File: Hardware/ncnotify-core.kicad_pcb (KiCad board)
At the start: 4 copper layers, 62.5 x 32.5 mm, 48 parts, among them J1 5-1634503-1, J2 67996-412HLF, J3 USB4110-GF-A, J4 Conn_ARM_JTAG_SWD_10, Q1 NX3008NBKS, SW1 SW_Push, SW2 SW_Push, U1 STM32L422CBT6, U2 TLV71333PDBV, X1 SMTU1632-LF, Y1 Q13FC1350000400

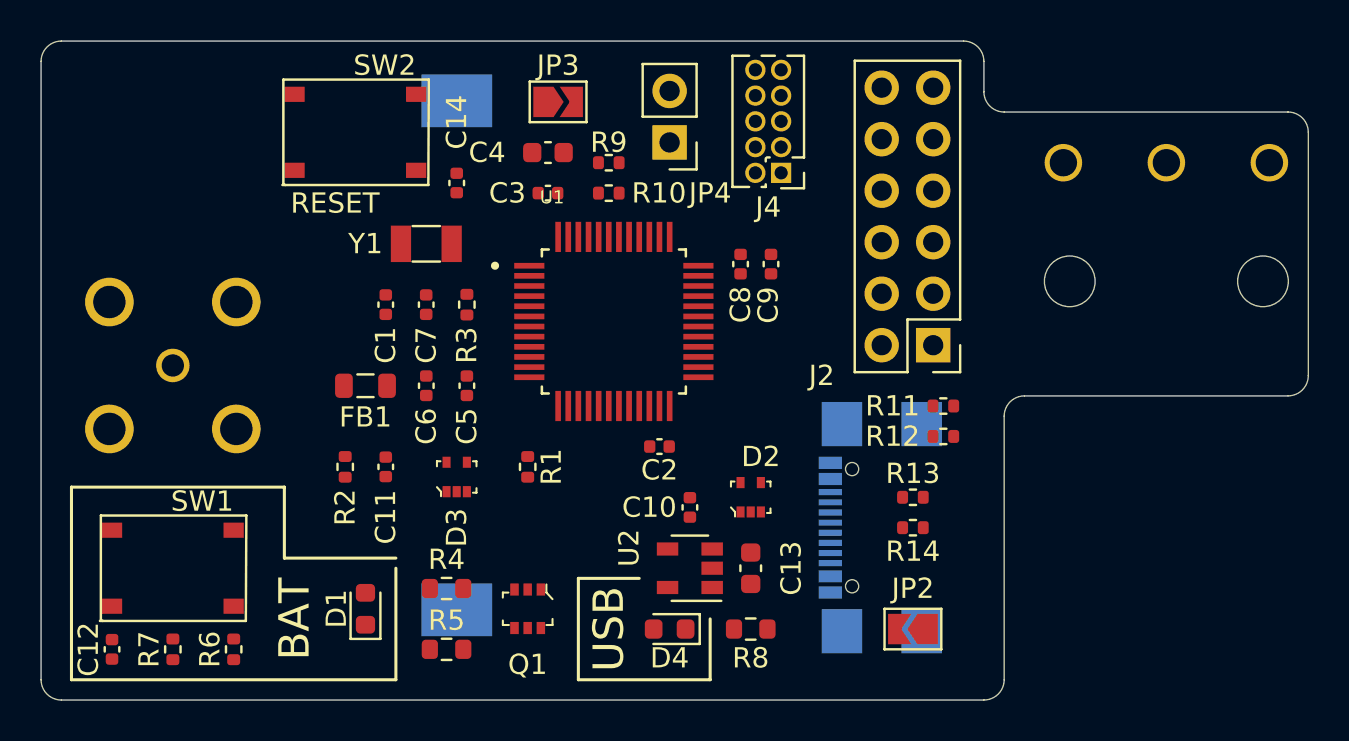
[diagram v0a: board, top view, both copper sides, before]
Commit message: Remove switches and expansion header
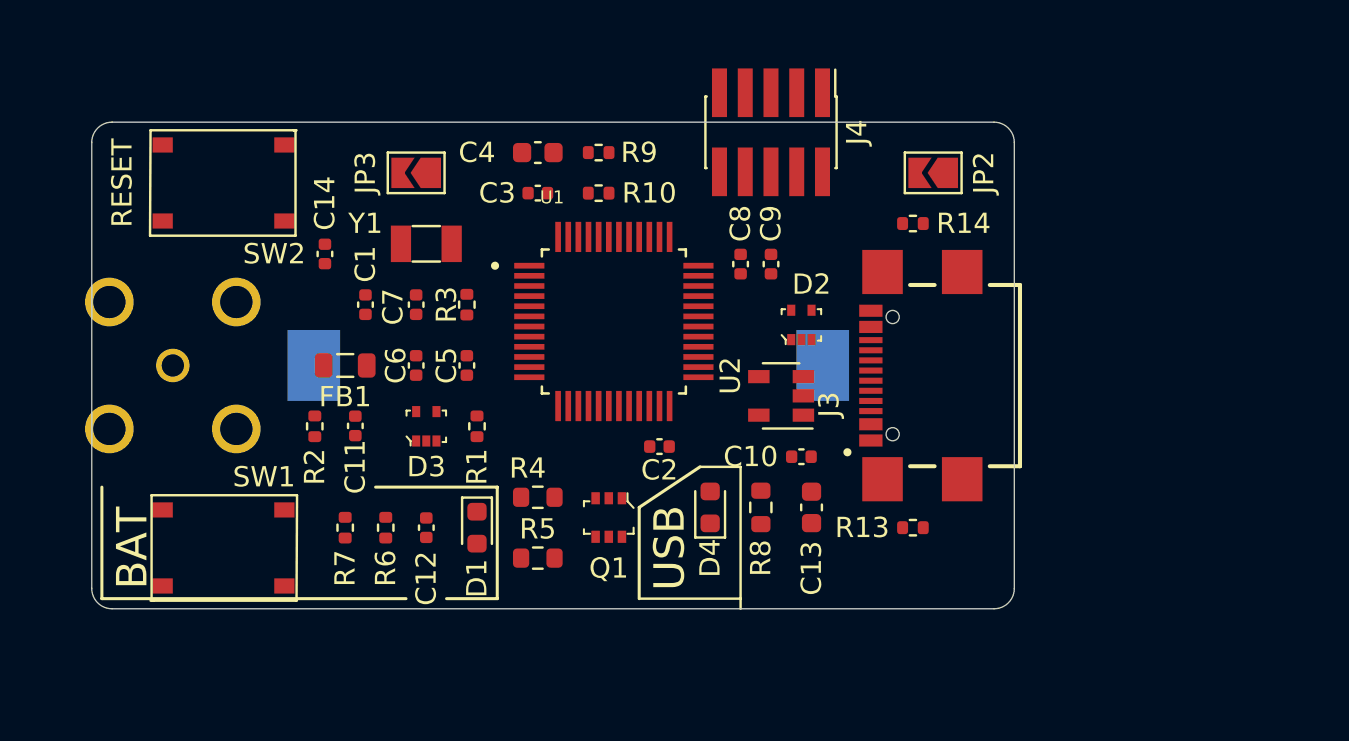
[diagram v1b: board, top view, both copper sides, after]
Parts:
- removed J2: 67996-412HLF, Connector_PinHeader_2.54mm:PinHeader_2x06_P2.54mm_Vertical
- removed JP4: Jumper_2_Open, Connector_PinHeader_2.54mm:PinHeader_1x02_P2.54mm_Vertical
- removed R11, R12: 5k1, Resistor_SMD:R_0402_1005Metric
- removed S1: ZMSL03130T10LLC, ncnotify-core:ZMSL03130T10LLC
- J3: moved to F.Cu
- J4: footprint Connector_PinHeader_1.27mm:PinHeader_2x05_P1.27mm_Vertical -> Connector_PinHeader_1.27mm:PinHeader_2x05_P1.27mm_Vertical_SMD
- moved JP2 22.5 mm to (249.0, -47.5)
- moved C12 16.6 mm to (224.0, -30.0), turned to 270 degrees
- moved R14 15.0 mm to (248.0, -45.0), turned to 0 degrees
- moved R7 10.4 mm to (220.0, -30.0), turned to 270 degrees
- moved U2 9.62 mm to (241.5, -36.5)
- moved R6 9.60 mm to (222.0, -30.0), turned to 270 degrees
- moved D2 8.86 mm to (242.5, -40.0)
- moved JP3 7.83 mm to (223.5, -47.5), turned to 180 degrees
- moved J3 7.76 mm to (247.0, -37.5), turned to 90 degrees
- moved C14 7.38 mm to (219.0, -43.5), turned to 90 degrees
- moved SW2 6.96 mm to (214.0, -47.0), turned to 180 degrees
- moved D1 6.80 mm to (226.5, -30.0), turned to 270 degrees
- moved R4 6.36 mm to (229.5, -31.5)
- moved R5 6.36 mm to (229.5, -28.5)
- moved D4 6.32 mm to (238.0, -31.0), turned to 90 degrees
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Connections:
- D2 pad 3: D+ -> D-
- D2 pad 5: D- -> D+
- R10 pad 1: Net-(JP4-Pad1) -> Net-(R10-Pad1)
- R9 pad 1: Net-(R9-Pad1) -> VDD
- R9 pad 2: Net-(JP4-Pad1) -> Net-(R10-Pad1)
- U1 pad 44: Net-(R9-Pad1) -> Net-(R10-Pad1)
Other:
- board size 62.5 x 32.5 mm -> 45.5 x 24 mm

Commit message: Routing and replaced USB ESD chip
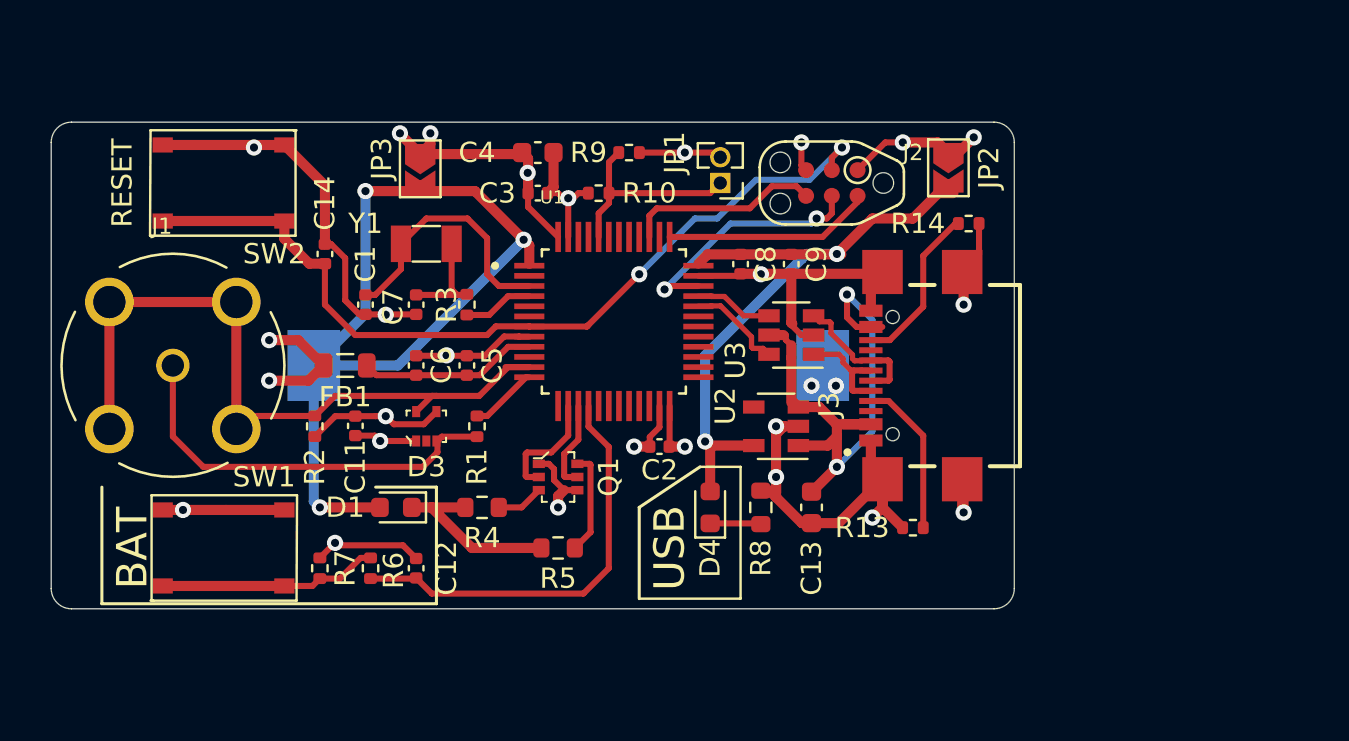
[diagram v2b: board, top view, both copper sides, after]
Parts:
- removed C10: 100n, Capacitor_SMD:C_0402_1005Metric
- removed D2: TPD2E001DRLR, digikey-footprints:SOT-553
- removed J4: Conn_ARM_JTAG_SWD_10, Connector_PinHeader_1.27mm:PinHeader_2x05_P1.27mm_Vertical_SMD
- added J2: TC2030-CTX, libs:TC2030-IDC-NL, F.Cu at (244.0, -47.0)
- added JP1: Jumper_2_Open, Connector_PinHeader_1.27mm:PinHeader_1x02_P1.27mm_Vertical, F.Cu at (238.5, -47.0)
- added U3: USBLC6-2SC6, Package_TO_SOT_SMD:SOT-23-6, F.Cu at (242.0, -39.5)
- J1: moved to F.Cu
- moved D1 4.12 mm to (222.5, -31.0), turned to 180 degrees
- moved Q1 3.20 mm to (230.5, -32.5), turned to 270 degrees
- moved R4 2.80 mm to (226.8, -31.0)
- moved R14 2.75 mm to (250.8, -45.0), turned to 180 degrees
- moved R7 2.36 mm to (218.8, -28.0), turned to 90 degrees
- moved R6 2.14 mm to (221.2, -28.0), turned to 90 degrees
- moved C12 2.06 mm to (223.5, -28.0), turned to 90 degrees
- moved U2 1.52 mm to (241.2, -35.0)
- moved R9 1.50 mm to (234.0, -48.5), turned to 180 degrees
- moved R5 1.12 mm to (230.5, -29.0)
- moved C9 1.00 mm to (242.0, -43.0)
- moved JP2 0.79 mm to (249.8, -47.8), turned to 270 degrees
- moved JP3 0.28 mm to (223.7, -47.7), turned to 270 degrees
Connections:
- J3 pad A6: D+ -> CONN_D+
- J3 pad A7: D- -> CONN_D-
- J3 pad B6: D+ -> CONN_D+
- J3 pad B7: D- -> CONN_D-
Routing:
- net GND: track 0.00 -> 101.7 mm, vias 0 -> 17
- net VBAT: track 0.00 -> 45.4 mm, vias 0 -> 3
- net NRST: track 0.00 -> 42.8 mm, vias 0 -> 2
- net VDD: track 0.00 -> 41.6 mm, vias 0 -> 11
- net S-: track 0.00 -> 37.0 mm
- net VBUS: track 0.00 -> 33.5 mm, vias 0 -> 2
- net VUSB: track 0.00 -> 29.4 mm, vias 0 -> 2
- net STATUS_READ: track 0.00 -> 21.0 mm
- net S+: track 0.00 -> 20.1 mm
- net OSC+: track 0.00 -> 12.8 mm
- net JTMS-SWDIO: track 0.00 -> 12.4 mm, vias 0 -> 2
- net Net-(R6-Pad2): track 0.00 -> 10.8 mm
- net JTCK-SWCLK: track 0.00 -> 10.3 mm
- net Net-(JP1-Pad1): track 0.00 -> 10.3 mm
- net JTDO: track 0.00 -> 9.58 mm
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- added copper zone on In1.Cu, net GND
- added copper zone on In2.Cu, net VDD
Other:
- board size 45.5 x 24 mm -> 47.5 x 24 mm
- board text added: "NCNotify Data Logger Bowen Shaner"

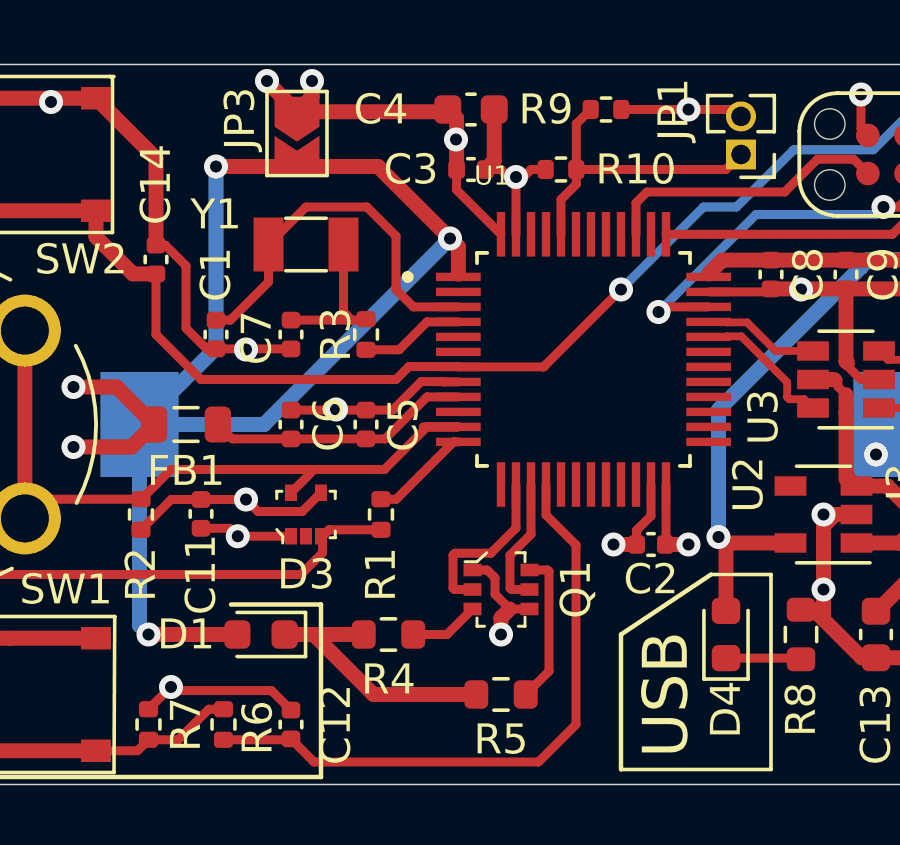
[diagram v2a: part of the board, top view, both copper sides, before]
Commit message: Routing and replaced USB ESD chip
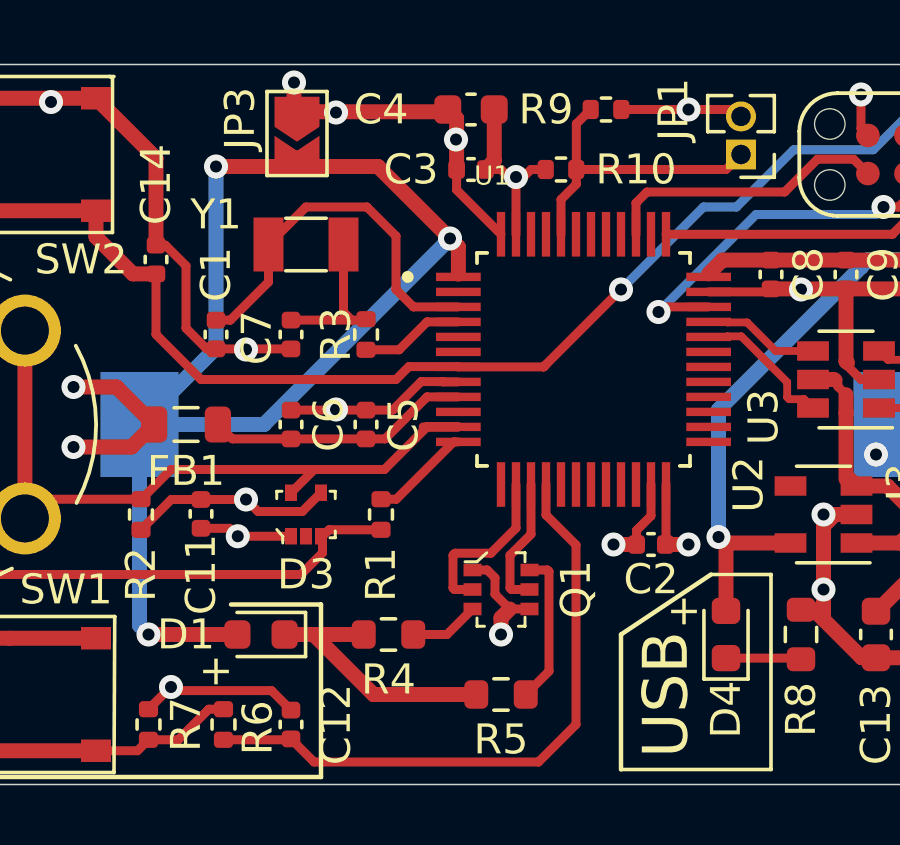
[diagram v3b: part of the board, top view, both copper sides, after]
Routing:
- net VDD: track 41.6 -> 39.9 mm
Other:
- board text added: "+"
- board text added: "JLCJLCJLCJLC"
- board text added: "NCNotify Data Logger Bowen Shaner v1.0"
- board text removed: "NCNotify Data Logger Bowen Shaner"
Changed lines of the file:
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@@
   (general
     (thickness 1.6)
-    (drawings 22)
-    (tracks 404)
+    (drawings 25)
+    (tracks 402)
     (zones 0)
     (modules 43)
@@
     (pad_to_mask_clearance 0)
     (aux_axis_origin 0 0)
-    (visible_elements 7FFDFFFF)
+    (visible_elements 7FFFFF7F)
     (pcbplotparams
       (layerselection 0x010fc_ffffffff)
@@
       (usegerberattributes true)
       (usegerberadvancedattributes true)
-      (creategerberjobfile true)
+      (creategerberjobfile false)
       (excludeedgelayer true)
       (linewidth 0.100000)
@@
       (outputformat 1)
       (mirror false)
-      (drillshape 1)
+      (drillshape 0)
       (scaleselection 1)
-      (outputdirectory ""))
+      (outputdirectory "../Production/gerber/"))
   )
   (net 0 "")
@@
   (module libs:QFP50P900X900X160-48N (layer F.Cu)
     (at 233.25 -40.17)
+    (attr smd)
     (fp_text reference U1 (at -3.048 -6.1214) (layer F.SilkS)
       (effects (font (size 0.64 0.64) (thickness 0.015)))
@@
     )
   )
-  (gr_text "NCNotify Data Logger\nBowen Shaner" (at 248.6 -38 90) (layer B.SilkS)
+  (gr_text + (at 221 -29.8) (layer F.SilkS)
+    (effects (font (size 1 1) (thickness 0.15)) (justify mirror))
+  )
+  (gr_text + (at 236.6 -31.8) (layer F.SilkS)
+    (effects (font (size 1 1) (thickness 0.15)) (justify mirror))
+  )
+  (gr_text JLCJLCJLCJLC (at 231.2 -38.2) (layer B.SilkS)
+    (effects (font (size 1 1) (thickness 0.15)) (justify mirror))
+  )
+  (gr_text "NCNotify Data Logger\nBowen Shaner\nv1.0" (at 249.2 -38 90) (layer B.SilkS)
     (effects (font (size 1 1) (thickness 0.15)) (justify mirror))
   )
@@
   (segment (start 238.27 -48.5) (end 238.5 -48.27) (width 0.3) (layer F.Cu) (net 3))
   (segment (start 234.51 -48.5) (end 236.75 -48.5) (width 0.3) (layer F.Cu) (net 3))
-  (segment (start 223.7 -48.425) (end 222.7 -49.425) (width 0.5) (layer F.Cu) (net 3))
-  (segment (start 222.7 -49.425) (end 222.7 -49.45) (width 0.5) (layer F.Cu) (net 3))
   (segment (start 221.5425 -37.52) (end 223.5 -37.52) (width 0.3) (layer F.Cu) (net 4))
   (segment (start 221.0625 -38) (end 221.5425 -37.52) (width 0.3) (layer F.Cu) (net 4))
@@
   (segment (start 214.125 -30.875) (end 217 -30.875) (width 0.5) (layer F.Cu) (net 3))
   (via (at 236.75 -34) (size 0.8) (drill 0.4) (layers F.Cu B.Cu) (net 3))
-  (via (at 222.7 -49.45) (size 0.8) (drill 0.4) (layers F.Cu B.Cu) (net 3))
-  (via (at 224.2 -49.45) (size 0.8) (drill 0.4) (layers F.Cu B.Cu) (net 3))
+  (via (at 223.6 -49.4) (size 0.8) (drill 0.4) (layers F.Cu B.Cu) (net 3))
+  (via (at 225 -48.4) (size 0.8) (drill 0.4) (layers F.Cu B.Cu) (net 3))
   (segment (start 236.75 -48.5) (end 238.27 -48.5) (width 0.3) (layer F.Cu) (net 3))
   (via (at 236.75 -48.5) (size 0.8) (drill 0.4) (layers F.Cu B.Cu) (net 3))
@@
   (segment (start 218.1875 -37.25) (end 218.9375 -38) (width 0.5) (layer F.Cu) (net 3))
   (segment (start 216.25 -37.25) (end 218.1875 -37.25) (width 0.5) (layer F.Cu) (net 3))
-  (segment (start 224.2 -48.925) (end 223.7 -48.425) (width 0.5) (layer F.Cu) (net 3))
-  (segment (start 224.2 -49.45) (end 224.2 -48.925) (width 0.5) (layer F.Cu) (net 3))
   (via (at 229 -47.5) (size 0.8) (drill 0.4) (layers F.Cu B.Cu) (net 3))
   (via (at 246 -30.5) (size 0.8) (drill 0.4) (layers F.Cu B.Cu) (net 1))
@@
   (segment (start 228.65 -48.425) (end 228.725 -48.5) (width 0.5) (layer F.Cu) (net 3))
   (segment (start 223.7 -48.425) (end 228.65 -48.425) (width 0.5) (layer F.Cu) (net 3))
+  (segment (start 223.6 -48.525) (end 223.7 -48.425) (width 0.5) (layer F.Cu) (net 3))
+  (segment (start 223.6 -49.4) (end 223.6 -48.525) (width 0.5) (layer F.Cu) (net 3))
   (via (at 237.75 -34.25) (size 0.8) (drill 0.4) (layers F.Cu B.Cu) (net 6))
   (segment (start 237.87999 -43.48) (end 237.42 -43.02001) (width 0.5) (layer F.Cu) (net 6))

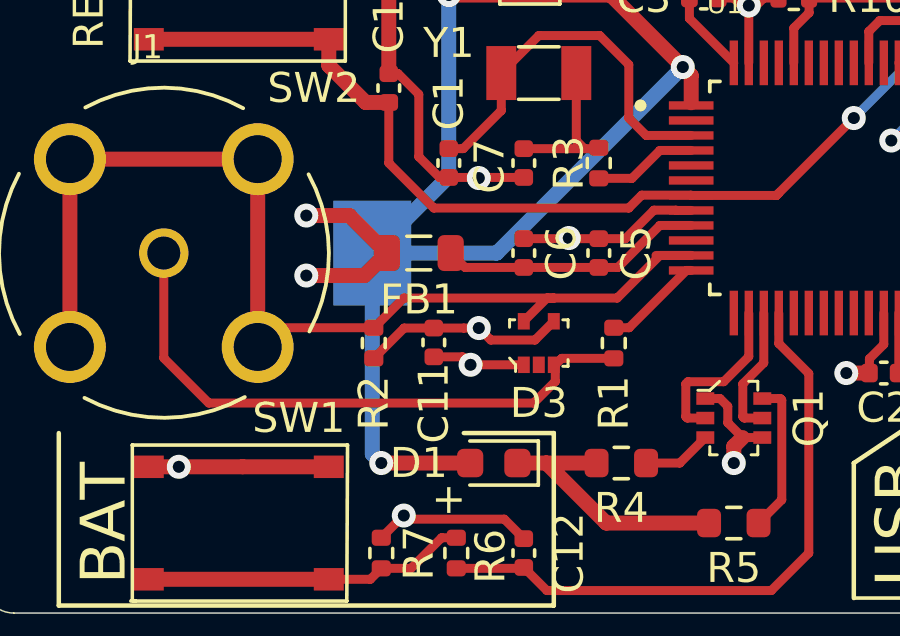
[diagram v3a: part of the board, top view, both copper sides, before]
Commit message: lcsc part numbers for bom, cleanup before trying gerbers
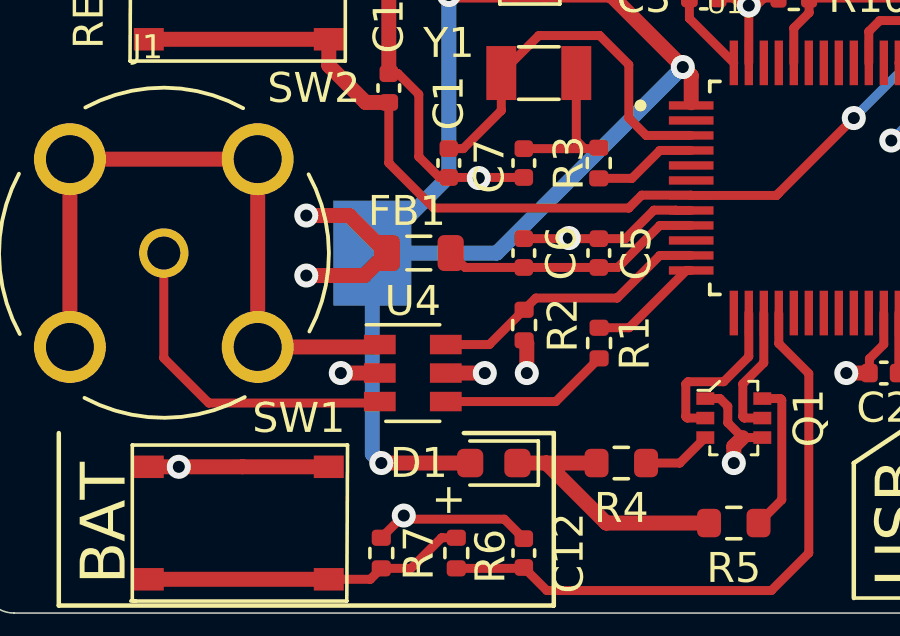
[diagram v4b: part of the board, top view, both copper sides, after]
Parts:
- removed C11: 100n, Capacitor_SMD:C_0402_1005Metric
- removed D3: TPD2E001DRLR, digikey-footprints:SOT-553
- added U4: USBLC6-2SC6, Package_TO_SOT_SMD:SOT-23-6, F.Cu at (219.8, -34.0)
- moved R2 5.05 mm to (223.5, -35.6)
- moved R1 0.49 mm to (226.0, -35.0)
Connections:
- R1 pad 1: SENSE_OUT -> GPIO_S+
- R1 pad 2: S+ -> SENSE_OUT
- R2 pad 2: S- -> GPIO_S-
- U1 pad 11: S- -> GPIO_S-
- U1 pad 12: SENSE_OUT -> GPIO_S+
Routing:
- net S-: track 37.0 -> 23.8 mm
- net GPIO_S-: track 0.00 -> 9.41 mm
- net S+: track 20.1 -> 11.3 mm
- net GND: track 101.7 -> 97.3 mm, vias 17 -> 18
- net GPIO_S+: track 0.00 -> 3.86 mm
- net SENSE_OUT: track 3.37 -> 5.71 mm
- net VDD: track 39.9 -> 38.2 mm
